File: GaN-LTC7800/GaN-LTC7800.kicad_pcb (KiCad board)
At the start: 2 copper layers, 63.5 x 46.5 mm, 40 parts, among them Q1 EPC2014C, Q2 EPC2014C, U1 LTC7800HUDC_PBF

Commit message: Updated for preassembly
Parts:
- added RLOAD2: 2Ohm, Resistor_SMD:R_0201_0603Metric, F.Cu at (116.9, 121.8)
- C1, C2, C3, C5, C6, COUT1, CSENSE1, CinA1, CinA2: footprint Capacitor_SMD:C_0805_2012Metric_Pad1.18x1.45mm_HandSolder -> Capacitor_SMD:C_0805_2012Metric
- CinB1: footprint Capacitor_SMD:C_0805_2012Metric_Pad1.18x1.45mm_HandSolder -> Capacitor_Tantalum_SMD:CP_EIA-7343-31_Kemet-D
- R1, R2, R4, R5, R6, R7, R9, RSENSE1: footprint Resistor_SMD:R_0201_0603Metric_Pad0.64x0.40mm_HandSolder -> Resistor_SMD:R_0201_0603Metric
- RLOAD1: value 5Ohm -> 3Ohm; footprint Resistor_SMD:R_0201_0603Metric_Pad0.64x0.40mm_HandSolder -> Resistor_SMD:R_0201_0603Metric
- moved RLOAD1 10.8 mm to (118.3, 121.8), turned to 180 degrees
- moved CinB1 3.66 mm to (111.6, 158.4), turned to 0 degrees
- moved VOUT1 1.52 mm to (120.9, 124.5)
- moved R5 1.06 mm to (125.9, 143.1)
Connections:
- RLOAD1 pad 2: GND -> Net-(RLOAD1-Pad2)
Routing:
- net Net-(RLOAD1-Pad2): track 0.00 -> 0.93 mm

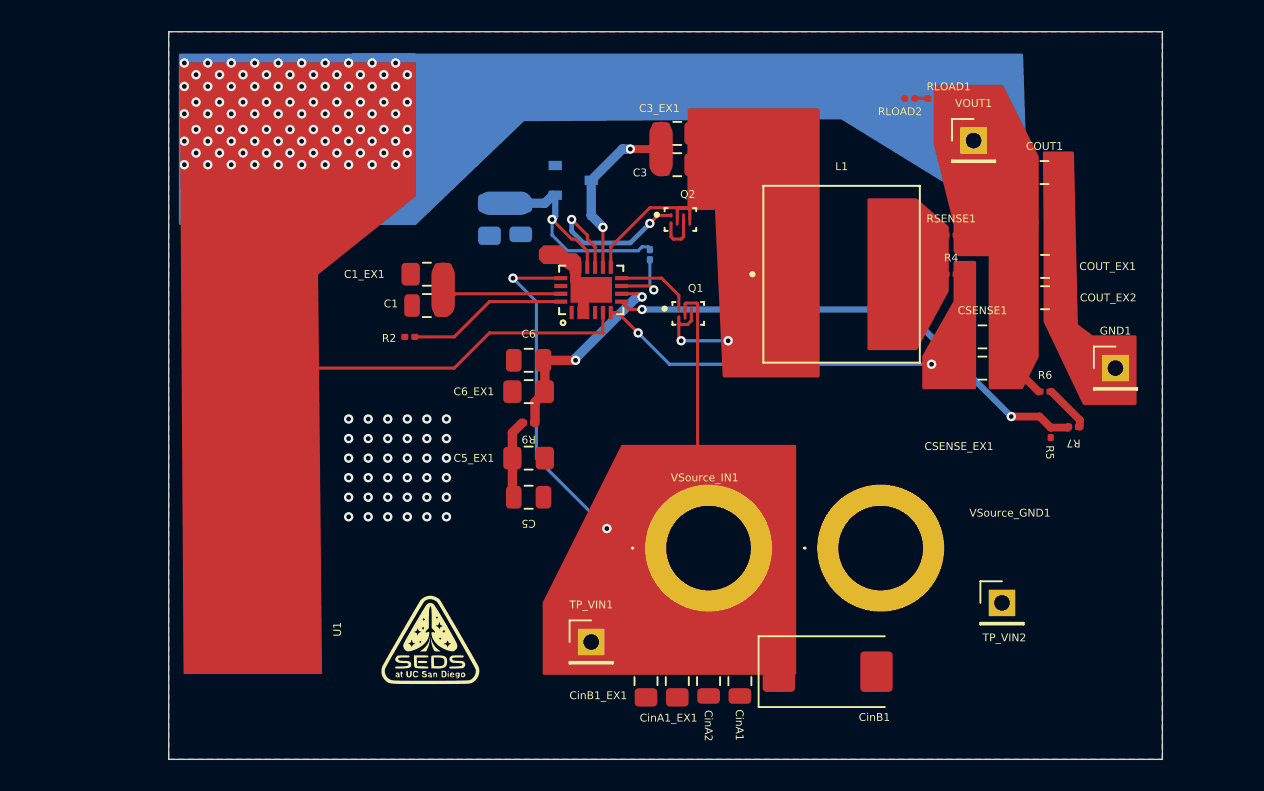
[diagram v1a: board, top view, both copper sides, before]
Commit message: mounting holes
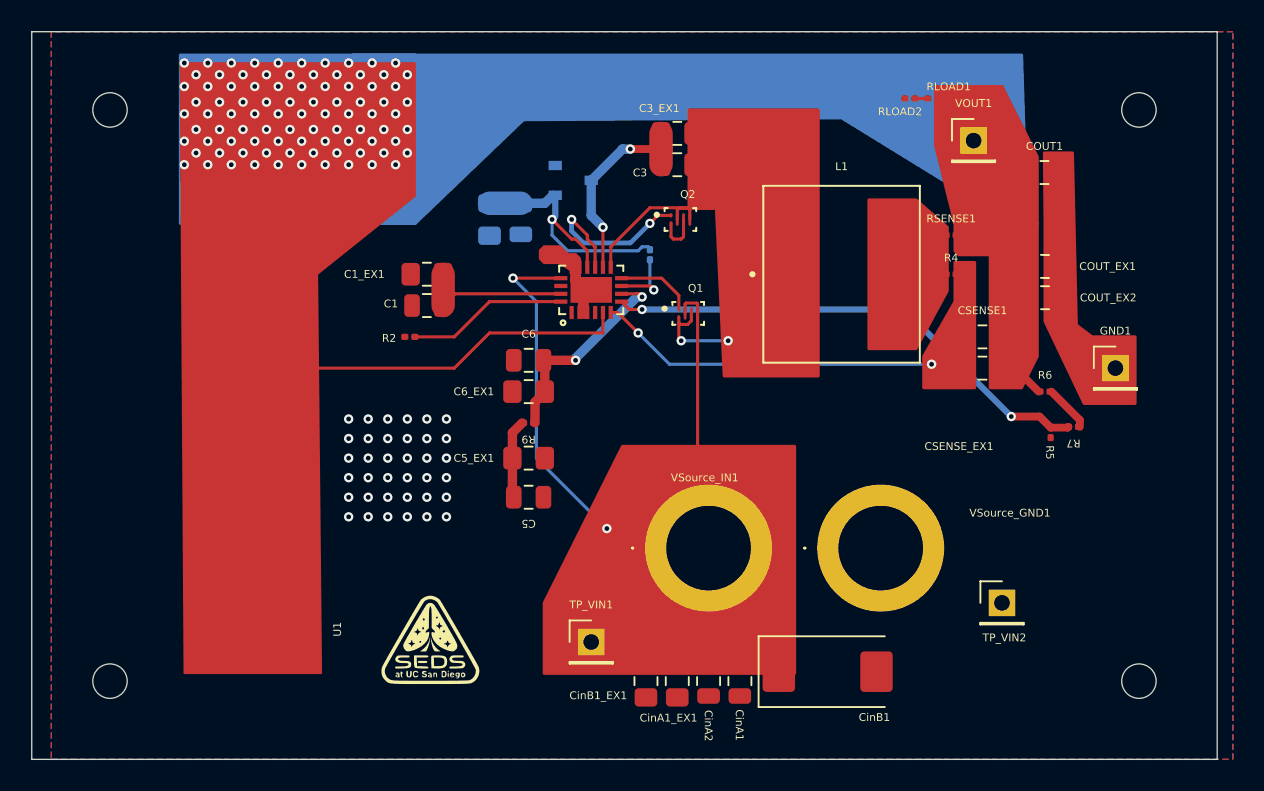
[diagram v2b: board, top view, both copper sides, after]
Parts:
- added REF**: MountingHole_2.2mm_M2, MountingHole:MountingHole_2.2mm_M2, F.Cu at (131.5, 159.0)
- added REF**: MountingHole_2.2mm_M2, MountingHole:MountingHole_2.2mm_M2, F.Cu at (131.5, 122.5)
- added REF**: MountingHole_2.2mm_M2, MountingHole:MountingHole_2.2mm_M2, F.Cu at (65.8, 159.0)
- added REF**: MountingHole_2.2mm_M2, MountingHole:MountingHole_2.2mm_M2, F.Cu at (65.8, 122.5)
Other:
- board size 63.5 x 46.5 mm -> 75.8 x 46.5 mm

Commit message: minor edits
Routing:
- net /BG: track 11.8 -> 7.17 mm
- net /INTVCC: track 18.0 -> 14.3 mm
- net Net-(U1-PGOOD): track 4.10 -> 3.23 mm
- net /ITH: track 13.6 -> 12.9 mm
